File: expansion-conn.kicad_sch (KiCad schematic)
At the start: 8 parts, among them J1 J_ERM8-040-05.0-L-DV-L-K-TR_S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

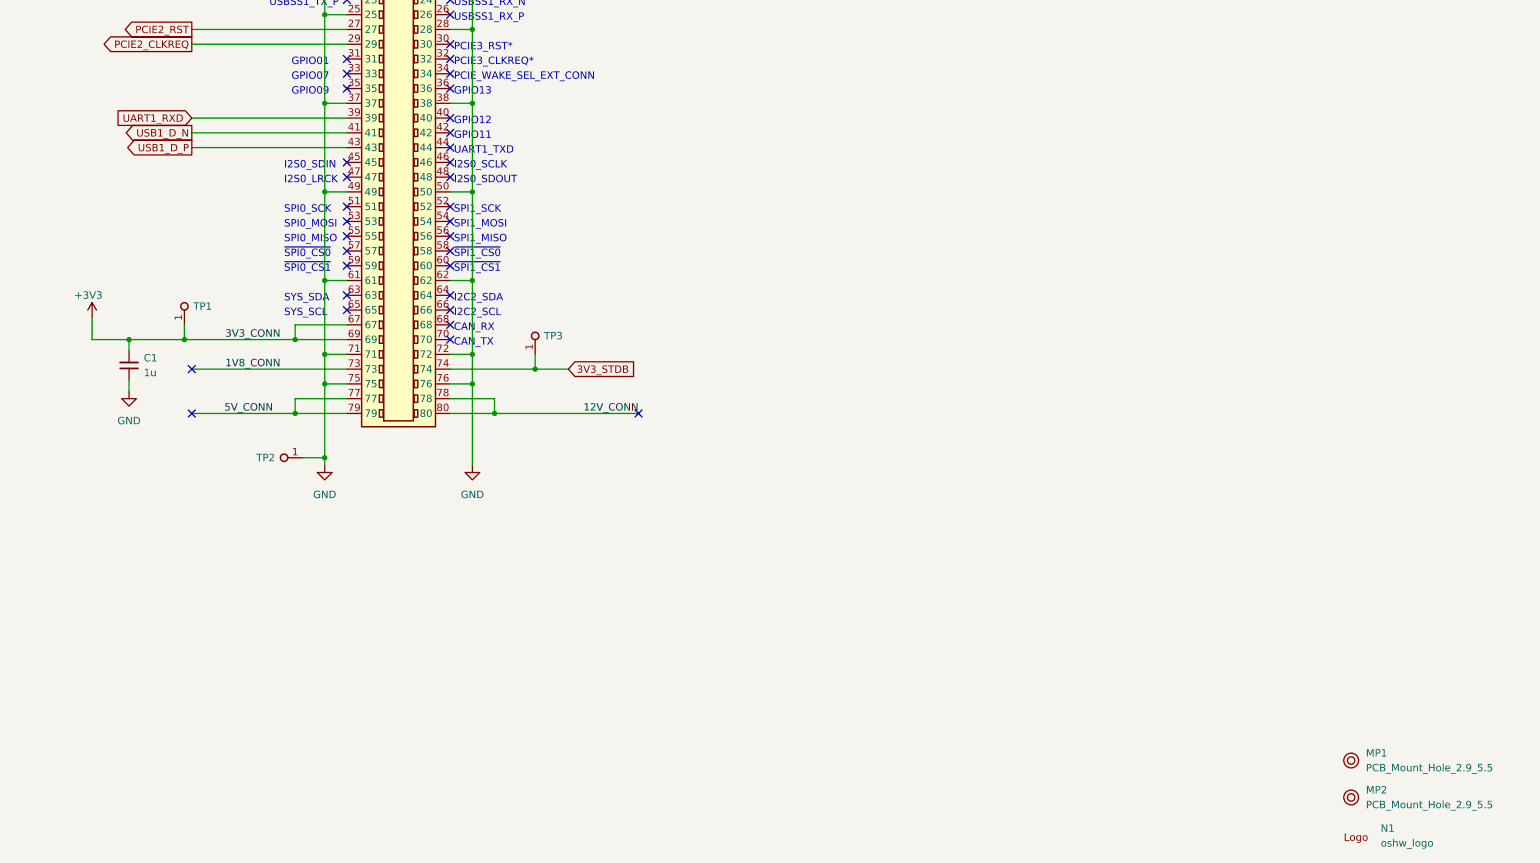
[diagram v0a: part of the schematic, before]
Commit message: [#49775] Cleanup net lists
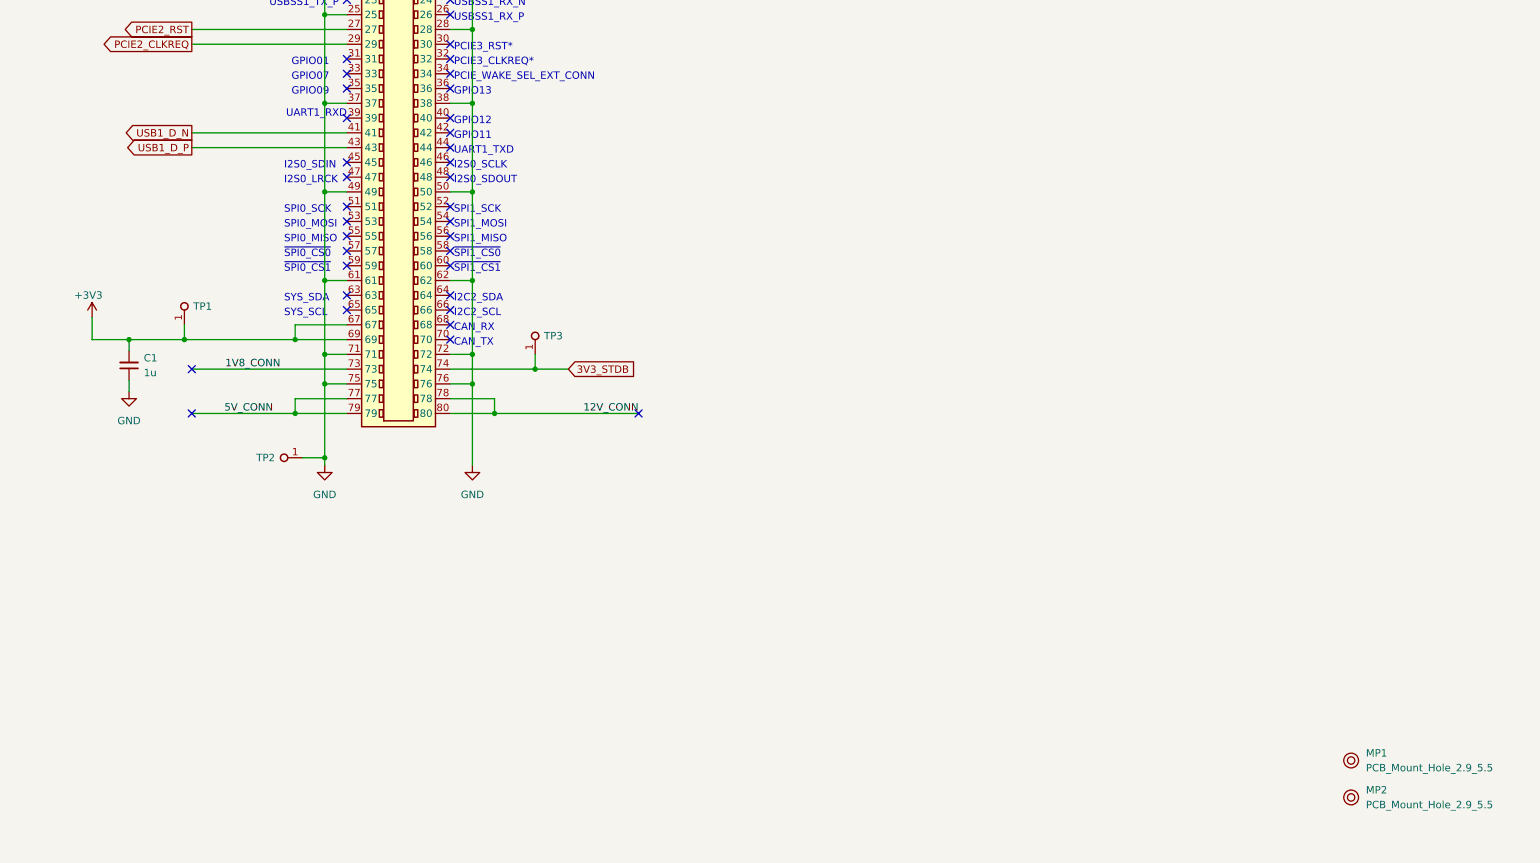
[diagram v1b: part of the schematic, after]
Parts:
- removed N1: oshw_logo, antmicro-footprints:oshw-logo, symbol antmicroMechanicalParts:oshw_logo
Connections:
- net UART1_RXD: no longer names the net of J1.39
- no-connect marks 39 -> 40
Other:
- note added: "UART1_RXD"
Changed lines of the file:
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@@
   (no_connect (at 218.44 95.25))
   (no_connect (at 200.66 156.21))
+  (no_connect (at 200.66 123.19))
   (no_connect (at 218.44 133.35))
   (no_connect (at 218.44 143.51))
@@
   )
   (wire (pts (xy 222.25 77.47) (xy 222.25 74.93))
-    (stroke (width 0) (type default) (color 0 0 0 0))
-  )
-  (wire (pts (xy 173.99 123.19) (xy 200.66 123.19))
     (stroke (width 0) (type default) (color 0 0 0 0))
   )
@@
     (effects (font (size 1.27 1.27)) (justify left bottom))
   )
+  (text "UART1_RXD" (at 200.66 123.19 180)
+    (effects (font (size 1.27 1.27)) (justify right bottom))
+  )
   (text "SYS_SDA" (at 189.865 154.94 0)
     (effects (font (size 1.27 1.27)) (justify left bottom))
@@
   )
   (label "12V_CONN" (at 250.825 173.99 180)
-    (effects (font (size 1.27 1.27)) (justify right bottom))
-  )
-  (label "3V3_CONN" (at 189.23 161.29 180)
     (effects (font (size 1.27 1.27)) (justify right bottom))
   )
@@
     (effects (font (size 1.27 1.27)) (justify right))
     (property "Intersheet References" "${INTERSHEET_REFS}" (id 0) (at 162.0217 125.6506 0)
-      (effects (font (size 1.27 1.27)) (justify right))
-    )
-  )
-  (global_label "UART1_RXD" (shape input) (at 173.99 123.19 180) (fields_autoplaced)
-    (effects (font (size 1.27 1.27)) (justify right))
-    (property "Intersheet References" "${INTERSHEET_REFS}" (id 0) (at 160.9936 123.1106 0)
       (effects (font (size 1.27 1.27)) (justify right))
     )
@@
     (pin "2")
   )
-  (symbol (lib_id "antmicroMechanicalParts:oshw_logo") (at 372.11 247.65 0) (unit 1)
-    (in_bom no) (on_board yes) (fields_autoplaced)
-    (property "Reference" "N1" (id 0) (at 378.46 245.3575 0)
-      (effects (font (size 1.27 1.27) (thickness 0.15)) (justify left))
-    )
-    (property "Value" "oshw_logo" (id 1) (at 378.46 247.8975 0)
-      (effects (font (size 1.27 1.27) (thickness 0.15)) (justify left))
-    )
-    (property "Footprint" "antmicro-footprints:oshw-logo" (id 2) (at 387.35 257.81 0)
-      (effects (font (size 1.27 1.27) (thickness 0.15)) (justify left bottom) hide)
-    )
-    (property "Datasheet" "" (id 3) (at 387.35 260.35 0)
-      (effects (font (size 1.27 1.27) (thickness 0.15)) (justify left bottom) hide)
-    )
-    (property "Author" "Antmicro" (id 4) (at 387.35 262.89 0)
-      (effects (font (size 1.27 1.27) (thickness 0.15)) (justify left bottom) hide)
-    )
-    (property "License" "Apache-2.0" (id 5) (at 387.35 265.43 0)
-      (effects (font (size 1.27 1.27) (thickness 0.15)) (justify left bottom) hide)
-    )
-    (property "MPN" "" (id 6) (at 372.11 247.65 0)
-      (effects (font (size 1.27 1.27)) hide)
-    )
-    (property "Manufacturer" "" (id 7) (at 387.35 267.97 0)
-      (effects (font (size 1.27 1.27) (thickness 0.15)) (justify left bottom) hide)
-    )
-  )
   (symbol (lib_id "antmicropower:GND") (at 222.25 182.88 0) (unit 1)

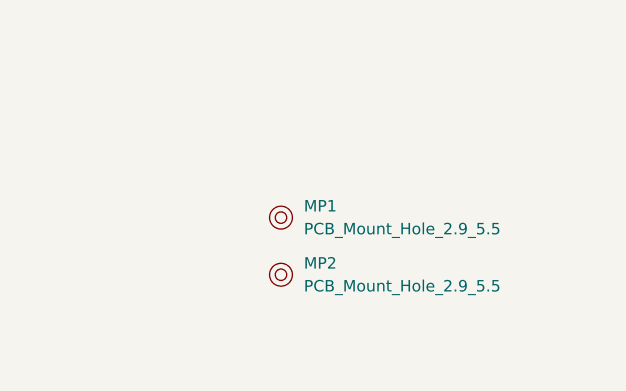
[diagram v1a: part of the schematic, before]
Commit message: [#49775] Update mounting holes with standarized components
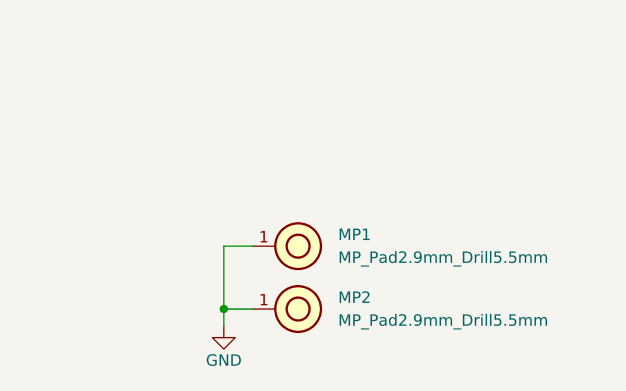
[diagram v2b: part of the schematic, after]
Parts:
- removed MP1, MP2: PCB_Mount_Hole_2.9_5.5, antmicro-footprints:mounting-hole-2.9mm-5.5mm, symbol antmicroMechanicalParts:PCB_Mount_Hole_2.9_5.5
- added MP1, MP2: MP_Pad2.9mm_Drill5.5mm, antmicro-footprints:MP_Pad2.9mm_Drill5.5mm, symbol antmicroMechanicalParts:MP_Pad2.9mm_Drill5.5mm
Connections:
- net GND: now also MP1.1, MP2.1
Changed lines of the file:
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@@
   (junction (at 222.25 163.83) (diameter 0) (color 0 0 0 0)
+  )
+  (junction (at 367.03 243.84) (diameter 0) (color 0 0 0 0)
   )
   (junction (at 222.25 100.33) (diameter 0) (color 0 0 0 0)
@@
     (stroke (width 0) (type default) (color 0 0 0 0))
   )
+  (wire (pts (xy 370.205 236.855) (xy 367.03 236.855))
+    (stroke (width 0) (type default) (color 0 0 0 0))
+  )
   (wire (pts (xy 218.44 166.37) (xy 233.045 166.37))
     (stroke (width 0) (type default) (color 0 0 0 0))
@@
     (stroke (width 0) (type default) (color 0 0 0 0))
   )
+  (wire (pts (xy 367.03 245.745) (xy 367.03 243.84))
+    (stroke (width 0) (type default) (color 0 0 0 0))
+  )
   (wire (pts (xy 173.99 87.63) (xy 200.66 87.63))
     (stroke (width 0) (type default) (color 0 0 0 0))
@@
     (stroke (width 0) (type default) (color 0 0 0 0))
   )
+  (wire (pts (xy 367.03 243.84) (xy 370.205 243.84))
+    (stroke (width 0) (type default) (color 0 0 0 0))
+  )
   (wire (pts (xy 218.44 120.65) (xy 222.25 120.65))
     (stroke (width 0) (type default) (color 0 0 0 0))
   )
   (wire (pts (xy 226.06 173.99) (xy 250.825 173.99))
+    (stroke (width 0) (type default) (color 0 0 0 0))
+  )
+  (wire (pts (xy 367.03 236.855) (xy 367.03 243.84))
     (stroke (width 0) (type default) (color 0 0 0 0))
   )
@@
     (pin "80")
   )
+  (symbol (lib_id "antmicroMechanicalParts:MP_Pad2.9mm_Drill5.5mm") (at 370.205 243.84 0) (unit 1)
+    (in_bom yes) (on_board yes) (fields_autoplaced)
+    (property "Reference" "MP2" (id 0) (at 379.73 242.5699 0)
+      (effects (font (size 1.27 1.27) (thickness 0.15)) (justify left))
+    )
+    (property "Value" "MP_Pad2.9mm_Drill5.5mm" (id 1) (at 379.73 245.1099 0)
+      (effects (font (size 1.27 1.27) (thickness 0.15)) (justify left))
+    )
+    (property "Footprint" "antmicro-footprints:MP_Pad2.9mm_Drill5.5mm" (id 2) (at 385.445 254 0)
+      (effects (font (size 1.27 1.27) (thickness 0.15)) (justify left bottom) hide)
+    )
+    (property "Datasheet" "" (id 3) (at 387.045 259.41 0)
+      (effects (font (size 1.27 1.27) (thickness 0.15)) (justify left bottom) hide)
+    )
+    (property "Author" "Antmicro" (id 4) (at 385.445 259.08 0)
+      (effects (font (size 1.27 1.27) (thickness 0.15)) (justify left bottom) hide)
+    )
+    (property "License" "Apache-2.0" (id 5) (at 385.445 261.62 0)
+      (effects (font (size 1.27 1.27) (thickness 0.15)) (justify left bottom) hide)
+    )
+    (pin "1")
+  )
+  (symbol (lib_id "antmicroMechanicalParts:MP_Pad2.9mm_Drill5.5mm") (at 370.205 236.855 0) (unit 1)
+    (in_bom yes) (on_board yes) (fields_autoplaced)
+    (property "Reference" "MP1" (id 0) (at 379.73 235.5849 0)
+      (effects (font (size 1.27 1.27) (thickness 0.15)) (justify left))
+    )
+    (property "Value" "MP_Pad2.9mm_Drill5.5mm" (id 1) (at 379.73 238.1249 0)
+      (effects (font (size 1.27 1.27) (thickness 0.15)) (justify left))
+    )
+    (property "Footprint" "antmicro-footprints:MP_Pad2.9mm_Drill5.5mm" (id 2) (at 385.445 247.015 0)
+      (effects (font (size 1.27 1.27) (thickness 0.15)) (justify left bottom) hide)
+    )
+    (property "Datasheet" "" (id 3) (at 387.045 252.425 0)
+      (effects (font (size 1.27 1.27) (thickness 0.15)) (justify left bottom) hide)
+    )
+    (property "Author" "Antmicro" (id 4) (at 385.445 252.095 0)
+      (effects (font (size 1.27 1.27) (thickness 0.15)) (justify left bottom) hide)
+    )
+    (property "License" "Apache-2.0" (id 5) (at 385.445 254.635 0)
+      (effects (font (size 1.27 1.27) (thickness 0.15)) (justify left bottom) hide)
+    )
+    (pin "1")
+  )
+  (symbol (lib_name "GND_1") (lib_id "antmicropower:GND") (at 367.03 245.745 0) (unit 1)
+    (in_bom yes) (on_board yes)
+    (property "Reference" "#PWR0101" (id 0) (at 375.92 248.285 0)
+      (effects (font (size 1.27 1.27) (thickness 0.15)) (justify left bottom) hide)
+    )
+    (property "Value" "GND" (id 1) (at 367.03 249.555 0)
+      (effects (font (size 1.27 1.27) (thickness 0.15)))
+    )
+    (property "Footprint" "" (id 2) (at 375.92 253.365 0)
+      (effects (font (size 1.27 1.27) (thickness 0.15)) (justify left bottom) hide)
+    )
+    (property "Datasheet" "" (id 3) (at 375.92 258.445 0)
+      (effects (font (size 1.27 1.27) (thickness 0.15)) (justify left bottom) hide)
+    )
+    (property "Author" "Antmicro" (id 4) (at 375.92 253.365 0)
+      (effects (font (size 1.27 1.27) (thickness 0.15)) (justify left bottom) hide)
+    )
+    (property "License" "Apache-2.0" (id 5) (at 375.92 255.905 0)
+      (effects (font (size 1.27 1.27) (thickness 0.15)) (justify left bottom) hide)
+    )
+    (pin "1")
+  )
   (symbol (lib_id "antmicroCapacitors0402:C_1u_0402") (at 163.195 168.275 90) (unit 1)
     (in_bom yes) (on_board yes) (fields_autoplaced)
@@
     (pin "1")
   )
-  (symbol (lib_id "antmicroMechanicalParts:PCB_Mount_Hole_2.9_5.5") (at 373.38 233.68 0) (mirror y) (unit 1)
-    (in_bom no) (on_board yes) (fields_autoplaced)
-    (property "Reference" "MP1" (id 0) (at 375.92 232.4099 0)
-      (effects (font (size 1.27 1.27) (thickness 0.15)) (justify right))
-    )
-    (property "Value" "PCB_Mount_Hole_2.9_5.5" (id 1) (at 375.92 234.9499 0)
-      (effects (font (size 1.27 1.27) (thickness 0.15)) (justify right))
-    )
-    (property "Footprint" "antmicro-footprints:mounting-hole-2.9mm-5.5mm" (id 2) (at 370.84 238.76 0)
-      (effects (font (size 1.27 1.27) (thickness 0.15)) (justify left bottom) hide)
-    )
-    (property "Datasheet" "" (id 3) (at 370.84 241.3 0)
-      (effects (font (size 1.27 1.27) (thickness 0.15)) (justify left bottom) hide)
-    )
-    (property "Author" "Antmicro" (id 4) (at 370.84 243.84 0)
-      (effects (font (size 1.27 1.27) (thickness 0.15)) (justify left bottom) hide)
-    )
-    (property "License" "Apache-2.0" (id 5) (at 370.84 246.38 0)
-      (effects (font (size 1.27 1.27) (thickness 0.15)) (justify left bottom) hide)
-    )
-  )
   (symbol (lib_id "antmicroTestPoints:TP_0.75mm_SMD") (at 193.04 181.61 0) (mirror y) (unit 1)
     (in_bom no) (on_board yes)
@@
     (pin "1")
   )
-  (symbol (lib_id "antmicroMechanicalParts:PCB_Mount_Hole_2.9_5.5") (at 373.38 240.03 0) (unit 1)
-    (in_bom no) (on_board yes)
-    (property "Reference" "MP2" (id 0) (at 375.92 238.76 0)
-      (effects (font (size 1.27 1.27) (thickness 0.15)) (justify left))
-    )
-    (property "Value" "PCB_Mount_Hole_2.9_5.5" (id 1) (at 375.92 241.3 0)
-      (effects (font (size 1.27 1.27) (thickness 0.15)) (justify left))
-    )
-    (property "Footprint" "antmicro-footprints:mounting-hole-2.9mm-5.5mm" (id 2) (at 375.92 245.11 0)
-      (effects (font (size 1.27 1.27) (thickness 0.15)) (justify left bottom) hide)
-    )
-    (property "Datasheet" "" (id 3) (at 375.92 247.65 0)
-      (effects (font (size 1.27 1.27) (thickness 0.15)) (justify left bottom) hide)
-    )
-    (property "Author" "Antmicro" (id 4) (at 375.92 250.19 0)
-      (effects (font (size 1.27 1.27) (thickness 0.15)) (justify left bottom) hide)
-    )
-    (property "License" "Apache-2.0" (id 5) (at 375.92 252.73 0)
-      (effects (font (size 1.27 1.27) (thickness 0.15)) (justify left bottom) hide)
-    )
-  )
   (symbol (lib_id "antmicropower:GND") (at 163.195 170.18 0) (unit 1)
